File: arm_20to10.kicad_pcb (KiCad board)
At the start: 2 copper layers, 5 parts, among them J1 ARM_20PIN, J2 ARM_10PIN, P1 +5V, P2 VCC, P3 GND

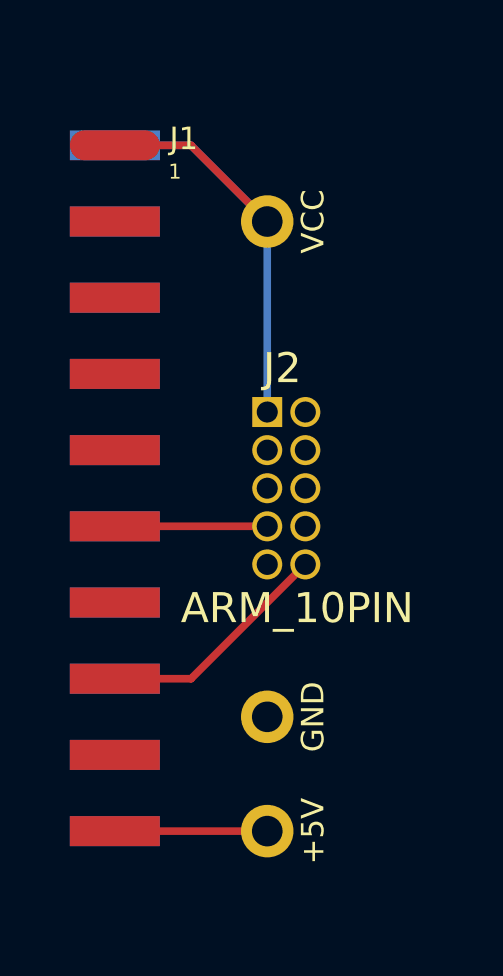
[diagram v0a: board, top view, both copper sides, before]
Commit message: - add gerbers, finish layout
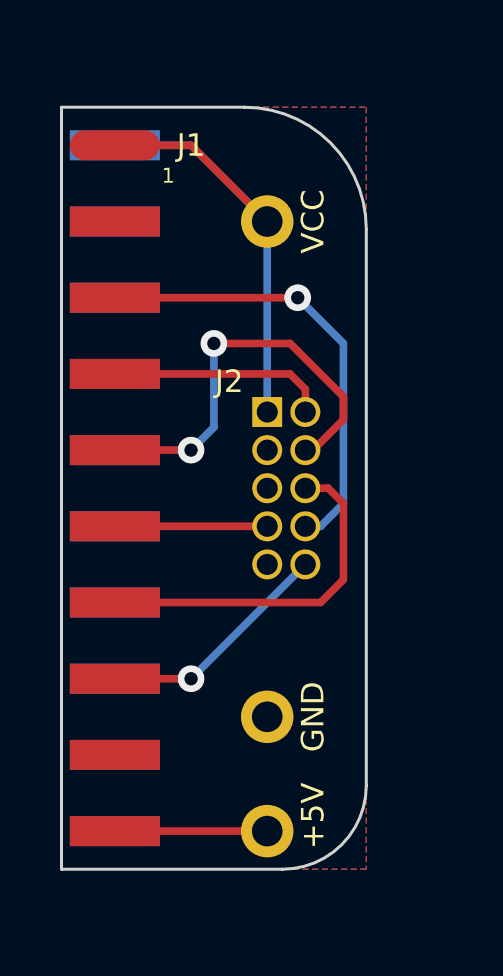
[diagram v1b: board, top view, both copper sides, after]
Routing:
- net TDI: track 0.00 -> 15.2 mm, vias 0 -> 1
- net TCLK/SWCLK: track 0.00 -> 13.9 mm, vias 0 -> 2
- net SWO/TDO: track 0.00 -> 12.0 mm
- net TMS/SWDIO: track 0.00 -> 7.32 mm
- net NRST: vias 0 -> 1
- added copper zone on B.Cu, net GND
- added copper zone on F.Cu, net GND
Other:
- board outline added: 10.2 x 25.4 mm
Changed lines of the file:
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@@
   (general
     (links 22)
-    (no_connects 16)
-    (area 0 0 0 0)
+    (no_connects 0)
+    (area 188.94552 121.354864 204.449 148.49221)
     (thickness 1.6)
-    (drawings 0)
-    (tracks 9)
+    (drawings 6)
+    (tracks 35)
     (zones 0)
     (modules 5)
@@
     (last_trace_width 0.254)
     (trace_clearance 0.254)
-    (zone_clearance 0.508)
+    (zone_clearance 0.254)
     (zone_45_only no)
     (trace_min 0.254)
@@
     (pad_to_mask_clearance 0)
     (aux_axis_origin 0 0)
-    (visible_elements 7FFFFFFF)
+    (visible_elements 7FFFFFBF)
     (pcbplotparams
-      (layerselection 3178497)
+      (layerselection 284196865)
       (usegerberextensions true)
       (excludeedgelayer true)
@@
       (outputformat 1)
       (mirror false)
-      (drillshape 1)
+      (drillshape 0)
       (scaleselection 1)
-      (outputdirectory ""))
+      (outputdirectory gerbers))
   )
   (net 0 "")
@@
       (effects (font (size 0.75 0.75) (thickness 0.12)))
     )
-    (fp_text value +5V (at 1.524 0 90) (layer F.SilkS)
+    (fp_text value +5V (at 1.524 -0.508 90) (layer F.SilkS)
       (effects (font (size 0.75 0.75) (thickness 0.12)))
     )
@@
   (module ARM_10_PIN (layer F.Cu)
     (at 198.12 134.62)
-    (fp_text reference J2 (at 0.5 -4) (layer F.SilkS)
-      (effects (font (size 1 1) (thickness 0.15)))
-    )
-    (fp_text value ARM_10PIN (at 1 4) (layer F.SilkS)
+    (fp_text reference J2 (at -1.27 -3.556) (layer F.SilkS)
+      (effects (font (size 0.75 0.75) (thickness 0.12)))
+    )
+    (fp_text value ARM_10PIN (at 1 4) (layer F.SilkS) hide
       (effects (font (size 1 1) (thickness 0.15)))
     )
@@
   (module ARM_20PIN_EDGE_BOTH (layer F.Cu)
     (at 193.04 128.27)
-    (fp_text reference J1 (at 2.30124 -5.30098) (layer F.SilkS)
-      (effects (font (size 0.7493 0.7493) (thickness 0.18796)))
+    (fp_text reference J1 (at 2.54 -5.08) (layer F.SilkS)
+      (effects (font (size 0.7493 0.7493) (thickness 0.12)))
     )
     (fp_text value ARM_20PIN (at 0 19.49958) (layer F.SilkS) hide
       (effects (font (size 0.7493 0.7493) (thickness 0.18796)))
     )
-    (fp_text user 1 (at 2.00152 -4.20116) (layer F.SilkS)
+    (fp_text user 1 (at 1.778 -4.064) (layer F.SilkS)
       (effects (font (size 0.50038 0.50038) (thickness 0.12446)))
     )
@@
     )
   )
+  (gr_line (start 191.262 147.32) (end 198.628 147.32) (angle 90) (layer Edge.Cuts) (width 0.1))
+  (gr_line (start 191.262 121.92) (end 191.262 147.32) (angle 90) (layer Edge.Cuts) (width 0.1))
+  (gr_line (start 201.422 125.984) (end 201.422 144.526) (angle 90) (layer Edge.Cuts) (width 0.1))
+  (gr_arc (start 197.358 125.984) (end 197.358 121.92) (angle 90) (layer Edge.Cuts) (width 0.1))
+  (gr_arc (start 198.628 144.526) (end 201.422 144.526) (angle 90) (layer Edge.Cuts) (width 0.1))
+  (gr_line (start 197.358 121.92) (end 191.262 121.92) (angle 90) (layer Edge.Cuts) (width 0.1))
   (segment (start 193.04 146.05) (end 198.12 146.05) (width 0.254) (layer F.Cu) (net 1))
   (segment (start 193.04 140.97) (end 195.58 140.97) (width 0.254) (layer F.Cu) (net 3))
-  (segment (start 195.58 140.97) (end 199.39 137.16) (width 0.254) (layer F.Cu) (net 3))
+  (segment (start 195.58 140.97) (end 199.39 137.16) (width 0.254) (layer B.Cu) (net 3))
+  (via (at 195.58 140.97) (size 0.889) (layers F.Cu B.Cu) (net 3))
   (segment (start 193.04 135.89) (end 198.12 135.89) (width 0.254) (layer F.Cu) (net 4))
+  (segment (start 193.04 138.43) (end 199.898 138.43) (width 0.254) (layer F.Cu) (net 5))
+  (segment (start 200.152 134.62) (end 199.39 134.62) (width 0.254) (layer F.Cu) (net 5))
+  (segment (start 200.66 135.128) (end 200.152 134.62) (width 0.254) (layer F.Cu) (net 5))
+  (segment (start 200.66 137.668) (end 200.66 135.128) (width 0.254) (layer F.Cu) (net 5))
+  (segment (start 199.898 138.43) (end 200.66 137.668) (width 0.254) (layer F.Cu) (net 5))
+  (segment (start 196.342 129.794) (end 198.882 129.794) (width 0.254) (layer F.Cu) (net 6))
+  (segment (start 198.882 129.794) (end 199.136 130.048) (width 0.254) (layer F.Cu) (net 6))
+  (segment (start 199.39 133.35) (end 199.644 133.35) (width 0.254) (layer F.Cu) (net 6))
+  (segment (start 195.58 133.35) (end 193.04 133.35) (width 0.254) (layer F.Cu) (net 6))
+  (via (at 195.58 133.35) (size 0.889) (layers F.Cu B.Cu) (net 6))
+  (segment (start 196.342 132.588) (end 195.58 133.35) (width 0.254) (layer B.Cu) (net 6))
+  (segment (start 196.342 129.794) (end 196.342 132.588) (width 0.254) (layer B.Cu) (net 6))
+  (via (at 196.342 129.794) (size 0.889) (layers F.Cu B.Cu) (net 6))
+  (segment (start 200.66 131.572) (end 199.136 130.048) (width 0.254) (layer F.Cu) (net 6))
+  (segment (start 200.66 132.334) (end 200.66 131.572) (width 0.254) (layer F.Cu) (net 6))
+  (segment (start 199.644 133.35) (end 200.66 132.334) (width 0.254) (layer F.Cu) (net 6))
+  (segment (start 199.39 135.89) (end 199.898 135.89) (width 0.254) (layer B.Cu) (net 7))
+  (segment (start 199.136 128.27) (end 193.04 128.27) (width 0.254) (layer F.Cu) (net 7))
+  (via (at 199.136 128.27) (size 0.889) (layers F.Cu B.Cu) (net 7))
+  (segment (start 200.66 129.794) (end 199.136 128.27) (width 0.254) (layer B.Cu) (net 7))
+  (segment (start 200.66 135.128) (end 200.66 129.794) (width 0.254) (layer B.Cu) (net 7))
+  (segment (start 199.898 135.89) (end 200.66 135.128) (width 0.254) (layer B.Cu) (net 7))
+  (segment (start 199.39 132.08) (end 199.39 131.318) (width 0.254) (layer F.Cu) (net 8))
+  (segment (start 198.882 130.81) (end 193.04 130.81) (width 0.254) (layer F.Cu) (net 8))
+  (segment (start 199.39 131.318) (end 198.882 130.81) (width 0.254) (layer F.Cu) (net 8))
   (segment (start 193.04 123.19) (end 195.58 123.19) (width 0.254) (layer F.Cu) (net 9))
   (segment (start 195.58 123.19) (end 198.12 125.73) (width 0.254) (layer F.Cu) (net 9))
@@
   (segment (start 195.58 123.19) (end 198.12 125.73) (width 0.254) (layer B.Cu) (net 9))
   (segment (start 198.12 132.08) (end 198.12 125.73) (width 0.254) (layer B.Cu) (net 9))
+  (zone (net 2) (net_name GND) (layer B.Cu) (hatch edge 0.508)
+    (connect_pads (clearance 0.254))
+    (min_thickness 0.254)
+    (fill (arc_segments 16) (thermal_gap 0.254) (thermal_bridge_width 0.508))
+    (polygon
+      (pts
+        (xy 201.422 147.32) (xy 191.262 147.32) (xy 191.262 121.92) (xy 201.422 121.92)
+      )
+    )
+  )
+  (zone (net 2) (net_name GND) (layer F.Cu) (hatch edge 0.508)
+    (connect_pads (clearance 0.254))
+    (min_thickness 0.254)
+    (fill (arc_segments 16) (thermal_gap 0.254) (thermal_bridge_width 0.508))
+    (polygon
+      (pts
+        (xy 201.422 147.32) (xy 191.262 147.32) (xy 191.262 121.92) (xy 201.422 121.92)
+      )
+    )
+  )
 )

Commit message: - layout done. add gnd next to vcc test point.
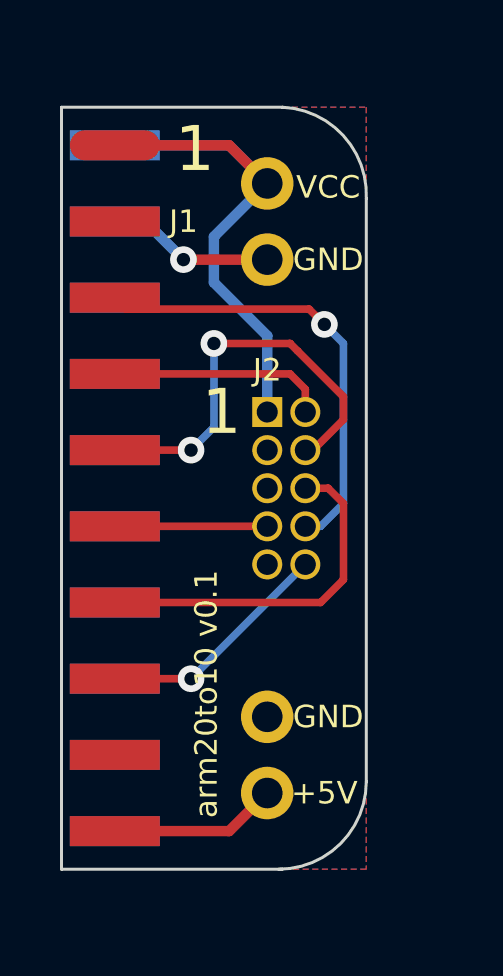
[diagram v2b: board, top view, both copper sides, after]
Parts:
- added P4: GND, TEST_0.100, F.Cu at (198.1, 127.0)
- moved P1 1.27 mm to (198.1, 144.8)
- moved P2 1.27 mm to (198.1, 124.5)
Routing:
- net GND: track 0.00 -> 5.61 mm, vias 0 -> 1
- net VCC: track 18.6 -> 20.3 mm
- net 5V: track 5.08 -> 5.61 mm
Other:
- outline, holes or cut-outs redrawn
- board text added: "1"
- board text added: "arm20to10 v0.1"
- board text added: "git.io/MUTo-A"
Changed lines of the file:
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@@
 (kicad_pcb (version 3) (host pcbnew "(2013-07-07 BZR 4022)-stable")
   (general
-    (links 22)
+    (links 23)
     (no_connects 0)
     (area 188.94552 121.354864 204.449 148.49221)
     (thickness 1.6)
-    (drawings 6)
-    (tracks 35)
+    (drawings 9)
+    (tracks 45)
     (zones 0)
-    (modules 5)
+    (modules 6)
     (nets 10)
   )
@@
   )
   (setup
-    (last_trace_width 0.254)
+    (last_trace_width 0.35)
+    (user_trace_width 0.35)
     (trace_clearance 0.254)
     (zone_clearance 0.254)
@@
   )
   (module TEST_0.100 (layer F.Cu)
-    (at 198.12 146.05)
+    (at 198.12 144.78)
     (fp_text reference P1 (at 0 -1.397) (layer F.SilkS) hide
       (effects (font (size 0.75 0.75) (thickness 0.12)))
     )
-    (fp_text value +5V (at 1.524 -0.508 90) (layer F.SilkS)
+    (fp_text value +5V (at 1.905 0) (layer F.SilkS)
       (effects (font (size 0.75 0.75) (thickness 0.12)))
     )
@@
   )
   (module TEST_0.100 (layer F.Cu)
-    (at 198.12 125.73)
+    (at 198.12 124.46)
     (fp_text reference P2 (at 0 -1.397) (layer F.SilkS) hide
       (effects (font (size 0.75 0.75) (thickness 0.12)))
     )
-    (fp_text value VCC (at 1.524 0 90) (layer F.SilkS)
+    (fp_text value VCC (at 2.032 0.127) (layer F.SilkS)
       (effects (font (size 0.75 0.75) (thickness 0.12)))
     )
@@
   (module ARM_10_PIN (layer F.Cu)
     (at 198.12 134.62)
-    (fp_text reference J2 (at -1.27 -3.556) (layer F.SilkS)
+    (fp_text reference J2 (at 0 -3.937) (layer F.SilkS)
       (effects (font (size 0.75 0.75) (thickness 0.12)))
     )
@@
       (effects (font (size 0.75 0.75) (thickness 0.12)))
     )
-    (fp_text value GND (at 1.524 0 90) (layer F.SilkS)
+    (fp_text value GND (at 2.032 0) (layer F.SilkS)
       (effects (font (size 0.75 0.75) (thickness 0.12)))
     )
@@
   (module ARM_20PIN_EDGE_BOTH (layer F.Cu)
     (at 193.04 128.27)
-    (fp_text reference J1 (at 2.54 -5.08) (layer F.SilkS)
+    (fp_text reference J1 (at 2.286 -2.54) (layer F.SilkS)
       (effects (font (size 0.7493 0.7493) (thickness 0.12)))
     )
@@
       (effects (font (size 0.7493 0.7493) (thickness 0.18796)))
     )
-    (fp_text user 1 (at 1.778 -4.064) (layer F.SilkS)
-      (effects (font (size 0.50038 0.50038) (thickness 0.12446)))
+    (fp_text user 1 (at 2.667 -4.953) (layer F.SilkS)
+      (effects (font (size 1.5 1.5) (thickness 0.2)))
     )
     (pad 3 smd rect (at 0 -2.54) (size 2.99974 1.00076)
@@
     )
   )
+  (module TEST_0.100 (layer F.Cu)
+    (at 198.12 127)
+    (fp_text reference P4 (at 0 -2.1) (layer F.SilkS) hide
+      (effects (font (size 0.75 0.75) (thickness 0.12)))
+    )
+    (fp_text value GND (at 2.032 0) (layer F.SilkS)
+      (effects (font (size 0.75 0.75) (thickness 0.12)))
+    )
+    (pad 1 thru_hole circle (at 0 0) (size 1.75 1.75) (drill 1.02)
+      (layers *.Cu *.Mask F.SilkS)
+      (net 2 GND)
+    )
+  )
+  (gr_text "arm20to10 v0.1" (at 196.088 141.478 90) (layer F.SilkS)
+    (effects (font (size 0.75 0.75) (thickness 0.12)))
+  )
+  (gr_text git.io/MUTo-A (at 200.152 142.367 90) (layer B.Mask)
+    (effects (font (size 0.75 0.65) (thickness 0.12)) (justify mirror))
+  )
+  (gr_text 1 (at 196.596 132.08) (layer F.SilkS)
+    (effects (font (size 1.5 1.5) (thickness 0.2)))
+  )
+  (gr_line (start 201.422 124.968) (end 201.422 144.399) (angle 90) (layer Edge.Cuts) (width 0.1))
+  (gr_line (start 191.262 121.92) (end 198.628 121.92) (angle 90) (layer Edge.Cuts) (width 0.1))
+  (gr_arc (start 198.501 124.841) (end 198.628 121.92) (angle 90) (layer Edge.Cuts) (width 0.1))
+  (gr_arc (start 198.501 144.399) (end 201.422 144.399) (angle 90) (layer Edge.Cuts) (width 0.1))
   (gr_line (start 191.262 147.32) (end 198.628 147.32) (angle 90) (layer Edge.Cuts) (width 0.1))
   (gr_line (start 191.262 121.92) (end 191.262 147.32) (angle 90) (layer Edge.Cuts) (width 0.1))
-  (gr_line (start 201.422 125.984) (end 201.422 144.526) (angle 90) (layer Edge.Cuts) (width 0.1))
-  (gr_arc (start 197.358 125.984) (end 197.358 121.92) (angle 90) (layer Edge.Cuts) (width 0.1))
-  (gr_arc (start 198.628 144.526) (end 201.422 144.526) (angle 90) (layer Edge.Cuts) (width 0.1))
-  (gr_line (start 197.358 121.92) (end 191.262 121.92) (angle 90) (layer Edge.Cuts) (width 0.1))
-  (segment (start 193.04 146.05) (end 198.12 146.05) (width 0.254) (layer F.Cu) (net 1))
+  (segment (start 193.04 146.05) (end 196.85 146.05) (width 0.35) (layer F.Cu) (net 1))
+  (segment (start 196.85 146.05) (end 198.12 144.78) (width 0.35) (layer F.Cu) (net 1))
+  (segment (start 195.326 127) (end 194.056 125.73) (width 0.35) (layer B.Cu) (net 2))
+  (via (at 195.326 127) (size 0.889) (layers F.Cu B.Cu) (net 2))
+  (segment (start 198.12 127) (end 195.326 127) (width 0.35) (layer F.Cu) (net 2))
+  (segment (start 194.056 125.73) (end 193.04 125.73) (width 0.35) (layer B.Cu) (net 2))
   (segment (start 193.04 140.97) (end 195.58 140.97) (width 0.254) (layer F.Cu) (net 3))
   (segment (start 195.58 140.97) (end 199.39 137.16) (width 0.254) (layer B.Cu) (net 3))
@@
   (segment (start 200.66 132.334) (end 200.66 131.572) (width 0.254) (layer F.Cu) (net 6))
   (segment (start 199.644 133.35) (end 200.66 132.334) (width 0.254) (layer F.Cu) (net 6))
+  (segment (start 199.517 128.651) (end 200.025 129.159) (width 0.254) (layer F.Cu) (net 7))
+  (segment (start 199.898 135.89) (end 200.66 135.128) (width 0.254) (layer B.Cu) (net 7))
+  (segment (start 200.66 135.128) (end 200.66 129.794) (width 0.254) (layer B.Cu) (net 7))
   (segment (start 199.39 135.89) (end 199.898 135.89) (width 0.254) (layer B.Cu) (net 7))
-  (segment (start 199.136 128.27) (end 193.04 128.27) (width 0.254) (layer F.Cu) (net 7))
-  (via (at 199.136 128.27) (size 0.889) (layers F.Cu B.Cu) (net 7))
-  (segment (start 200.66 129.794) (end 199.136 128.27) (width 0.254) (layer B.Cu) (net 7))
-  (segment (start 200.66 135.128) (end 200.66 129.794) (width 0.254) (layer B.Cu) (net 7))
-  (segment (start 199.898 135.89) (end 200.66 135.128) (width 0.254) (layer B.Cu) (net 7))
+  (segment (start 193.421 128.651) (end 199.517 128.651) (width 0.254) (layer F.Cu) (net 7))
+  (segment (start 193.421 128.651) (end 193.04 128.27) (width 0.254) (layer F.Cu) (net 7))
+  (segment (start 200.025 129.159) (end 200.66 129.794) (width 0.254) (layer B.Cu) (net 7))
+  (via (at 200.025 129.159) (size 0.889) (layers F.Cu B.Cu) (net 7))
   (segment (start 199.39 132.08) (end 199.39 131.318) (width 0.254) (layer F.Cu) (net 8))
   (segment (start 198.882 130.81) (end 193.04 130.81) (width 0.254) (layer F.Cu) (net 8))
   (segment (start 199.39 131.318) (end 198.882 130.81) (width 0.254) (layer F.Cu) (net 8))
-  (segment (start 193.04 123.19) (end 195.58 123.19) (width 0.254) (layer F.Cu) (net 9))
-  (segment (start 195.58 123.19) (end 198.12 125.73) (width 0.254) (layer F.Cu) (net 9))
-  (segment (start 193.04 123.19) (end 195.58 123.19) (width 0.254) (layer B.Cu) (net 9))
-  (segment (start 195.58 123.19) (end 198.12 125.73) (width 0.254) (layer B.Cu) (net 9))
-  (segment (start 198.12 132.08) (end 198.12 125.73) (width 0.254) (layer B.Cu) (net 9))
+  (segment (start 198.12 124.46) (end 196.342 126.238) (width 0.35) (layer B.Cu) (net 9))
+  (segment (start 198.12 129.54) (end 198.12 132.08) (width 0.35) (layer B.Cu) (net 9))
+  (segment (start 196.342 127.762) (end 198.12 129.54) (width 0.35) (layer B.Cu) (net 9))
+  (segment (start 196.342 126.238) (end 196.342 127.762) (width 0.35) (layer B.Cu) (net 9))
+  (segment (start 193.04 123.19) (end 196.85 123.19) (width 0.35) (layer B.Cu) (net 9))
+  (segment (start 196.85 123.19) (end 198.12 124.46) (width 0.35) (layer B.Cu) (net 9))
+  (segment (start 193.04 123.19) (end 196.85 123.19) (width 0.35) (layer F.Cu) (net 9))
+  (segment (start 196.85 123.19) (end 198.12 124.46) (width 0.35) (layer F.Cu) (net 9))
   (zone (net 2) (net_name GND) (layer B.Cu) (hatch edge 0.508)
     (connect_pads (clearance 0.254))

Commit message: - new layout w/ ldo + switch
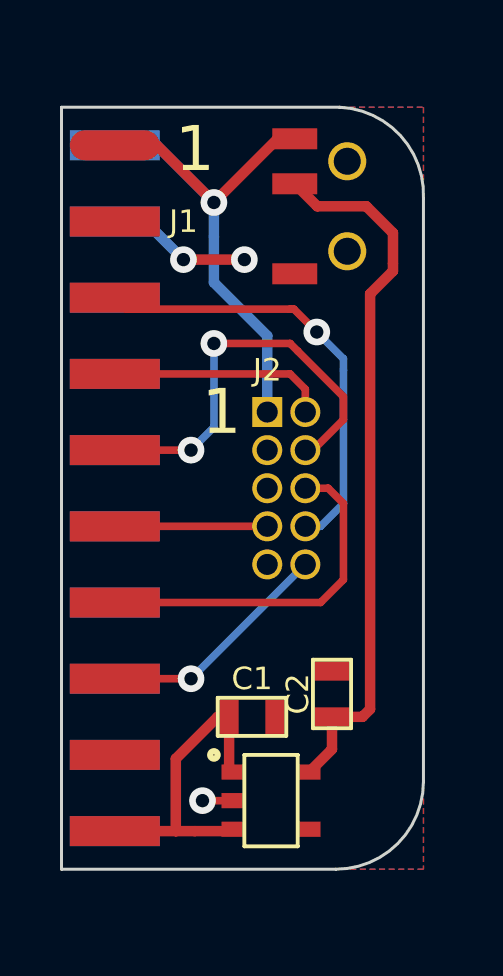
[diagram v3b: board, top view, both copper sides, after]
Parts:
- removed P1: +5V, TEST_0.100
- removed P2: VCC, TEST_0.100
- removed P3, P4: GND, TEST_0.100
- added C1: C, SM0603, F.Cu at (197.6, 142.2)
- added C2: C, SM0603, F.Cu at (200.3, 141.5)
- added SW1: DUAL_SWITCH_INV, SWITCH_SLIDE_SSSS810701, F.Cu at (200.8, 125.2)
- added U1: AAT3221 or LP5907, SOT23-5, F.Cu at (198.2, 145.0)
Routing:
- net N-000009: track 0.00 -> 23.7 mm
- net 5V: track 5.61 -> 10.5 mm
- net VCC: track 20.3 -> 19.8 mm, vias 0 -> 1
- net GND: track 5.61 -> 5.86 mm, vias 1 -> 3
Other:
- board size 10.2 x 25.4 mm -> 12.1 x 25.4 mm
- board text added: "arm20to10 v0.2 git.io/MUTo-A"
- board text removed: "arm20to10 v0.1"
- board text removed: "git.io/MUTo-A"

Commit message: - re layout with leds
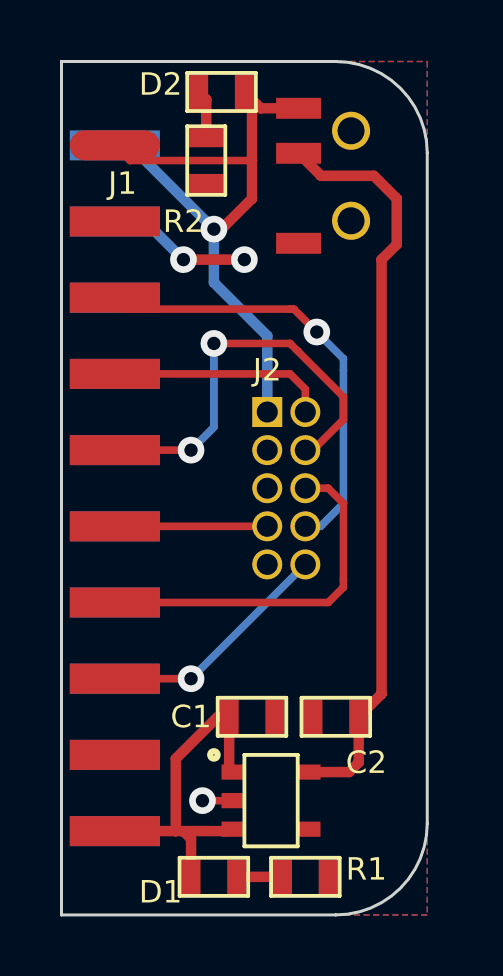
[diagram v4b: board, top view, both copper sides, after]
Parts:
- added D1: LED, SM0603, F.Cu at (196.3, 147.6)
- added D2: LED, SM0603, F.Cu at (196.6, 121.4)
- added R1: 1K, SM0603, F.Cu at (199.4, 147.6)
- added R2: 500R, SM0603, F.Cu at (196.1, 123.7)
- C1, C2: value C -> 1.0uF
- moved SW1 1.02 mm to (200.9, 124.2)
- moved C2 0.77 mm to (200.4, 142.2), turned to 180 degrees
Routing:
- net VCC: track 19.8 -> 23.5 mm
- net 5V: track 10.5 -> 12.1 mm
- net N-000007: track 0.00 -> 1.63 mm
- net N-000006: track 0.00 -> 1.52 mm
- net N-0000010: track 23.7 -> 25.0 mm
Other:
- board size 12.1 x 25.4 mm -> 12.2 x 28.4 mm
- board text added: "arm20to10 v0.3 git.io/MUTo-A"
- board text removed: "1"
- board text removed: "arm20to10 v0.2 git.io/MUTo-A"
